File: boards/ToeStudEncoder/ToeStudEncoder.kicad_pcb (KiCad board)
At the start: 2 copper layers, 11 parts, among them J2 ISP, J3 ToeLeft, J4 ToeRight, U1 ATmega48-20P, U2 6N138

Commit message: Renamed toestud encoder schematics
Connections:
- J3 pad 1: Net-(J3-Pad1) -> L1
- J3 pad 10: L3 -> Net-(U1-Pad5)
- J3 pad 2: unconnected-(J3-Pad2) -> Net-(U1-Pad13)
- J3 pad 3: Net-(J3-Pad3) -> unconnected-(J3-Pad3)
- J3 pad 4: unconnected-(J3-Pad4) -> Net-(U1-Pad12)
- J3 pad 5: Net-(J3-Pad5) -> unconnected-(J3-Pad5)
- J3 pad 6: unconnected-(J3-Pad6) -> Net-(U1-Pad11)
- J3 pad 7: Net-(J3-Pad7) -> unconnected-(J3-Pad7)
- J3 pad 8: MOSI -> Net-(U1-Pad6)
- J3 pad 9: Net-(J3-Pad9) -> L2
- J4 pad 1: Net-(J3-Pad1) -> L3
- J4 pad 10: L1 -> Net-(U1-Pad5)
- J4 pad 2: unconnected-(J4-Pad2) -> Net-(U1-Pad13)
- J4 pad 3: Net-(J3-Pad3) -> unconnected-(J4-Pad3)
- J4 pad 4: unconnected-(J4-Pad4) -> Net-(U1-Pad12)
- J4 pad 5: Net-(J3-Pad5) -> unconnected-(J4-Pad5)
- J4 pad 6: unconnected-(J4-Pad6) -> Net-(U1-Pad11)
- J4 pad 7: Net-(J3-Pad7) -> unconnected-(J4-Pad7)
- J4 pad 8: L2 -> Net-(U1-Pad6)
- J4 pad 9: Net-(J3-Pad9) -> MOSI
- U1 pad 11: Net-(J3-Pad5) -> Net-(U1-Pad11)
- U1 pad 12: Net-(J3-Pad7) -> Net-(U1-Pad12)
- U1 pad 13: Net-(J3-Pad9) -> Net-(U1-Pad13)
- U1 pad 5: Net-(J3-Pad1) -> Net-(U1-Pad5)
- U1 pad 6: Net-(J3-Pad3) -> Net-(U1-Pad6)

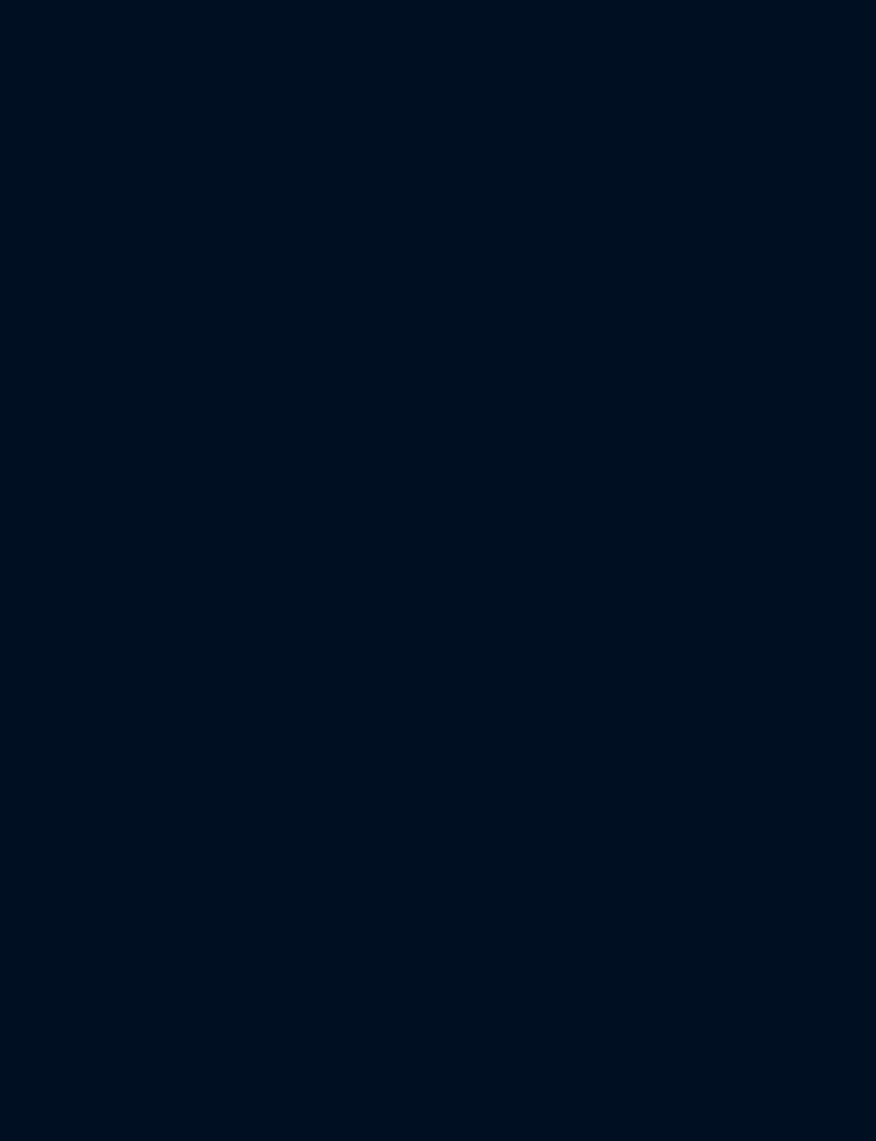
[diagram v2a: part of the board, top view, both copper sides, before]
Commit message: Updated to KiCAD 8, fixed optocouplers for MIDI and added powersupplies
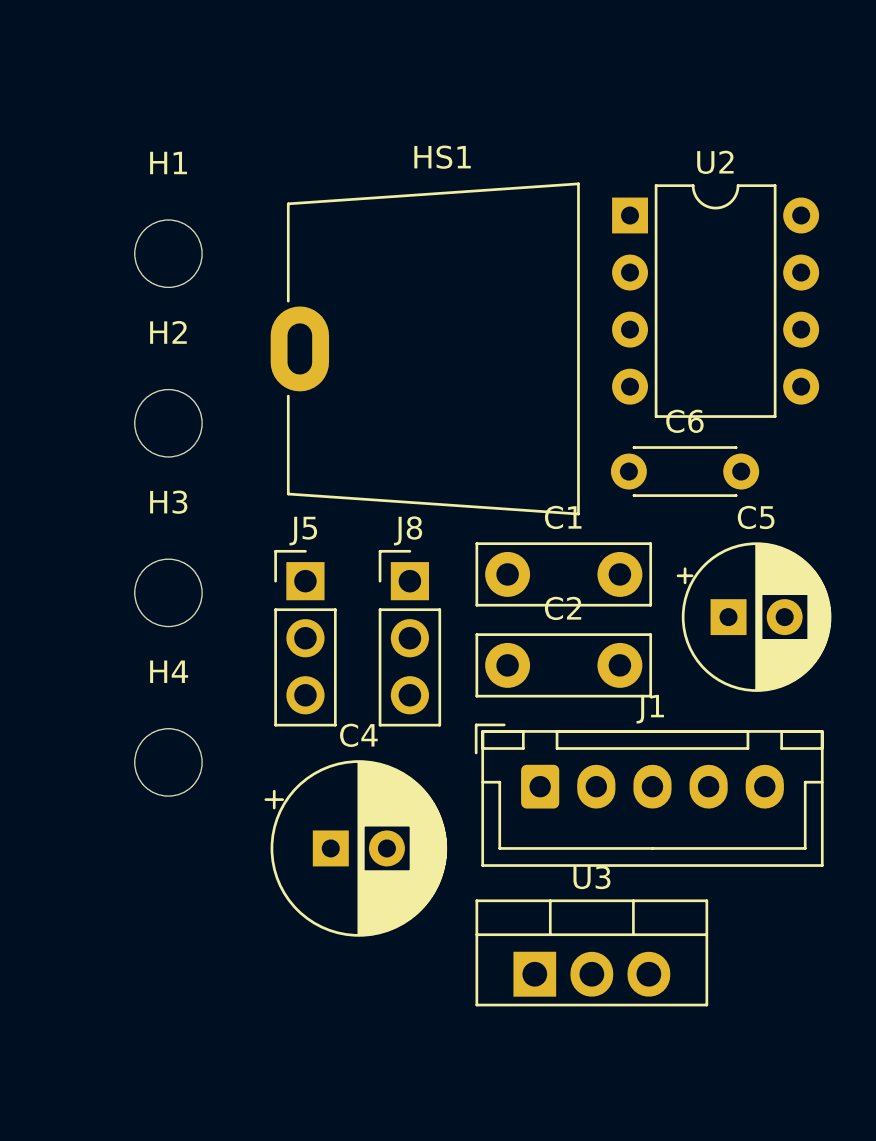
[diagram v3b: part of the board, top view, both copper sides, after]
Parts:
- added C1: 100nF, Capacitor_THT:C_Disc_D7.5mm_W2.5mm_P5.00mm, F.Cu at (233.0, 69.6)
- added C2: 100nF, Capacitor_THT:C_Disc_D7.5mm_W2.5mm_P5.00mm, F.Cu at (233.0, 73.6)
- added C4: 33uF, Capacitor_THT:CP_Radial_D7.5mm_P2.50mm, F.Cu at (225.1, 81.8)
- added C5: 10uF, Capacitor_THT:CP_Radial_D6.3mm_P2.50mm, F.Cu at (242.8, 71.5)
- added C6: 100nF, Capacitor_THT:C_Disc_D4.3mm_W1.9mm_P5.00mm, F.Cu at (238.4, 65.0)
- added H1: MountingHole, MountingHole:MountingHole_3mm, F.Cu at (217.9, 55.3)
- added H2: MountingHole, MountingHole:MountingHole_3mm, F.Cu at (217.9, 62.8)
- added H3: MountingHole, MountingHole:MountingHole_3mm, F.Cu at (217.9, 70.4)
- added H4: MountingHole, MountingHole:MountingHole_3mm, F.Cu at (217.9, 77.9)
- added HS1: Heatsink_Pad, Heatsink:Heatsink_AAVID_576802B03900G, F.Cu at (223.7, 59.5)
- added J1: Swell, Connector_JST:JST_XH_B5B-XH-A_1x05_P2.50mm_Vertical, F.Cu at (234.4, 79.0)
- added J5: MIDI In, Connector_PinHeader_2.54mm:PinHeader_1x03_P2.54mm_Vertical, F.Cu at (224.0, 69.9)
- added J8: MIDI Out, Connector_PinHeader_2.54mm:PinHeader_1x03_P2.54mm_Vertical, F.Cu at (228.6, 69.9)
- added U2: 6N137, Package_DIP:DIP-8_W7.62mm, F.Cu at (238.4, 53.6)
- added U3: L7805, Package_TO_SOT_THT:TO-220-3_Vertical, F.Cu at (234.2, 87.4)
- R1: value 10k -> 1k
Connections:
- D1 pad 1: Net-(D1-Pad1) -> Net-(D1-K)
- D1 pad 2: Net-(D1-Pad2) -> Net-(D1-A)
- R5 pad 2: Net-(D1-Pad1) -> Net-(D1-K)

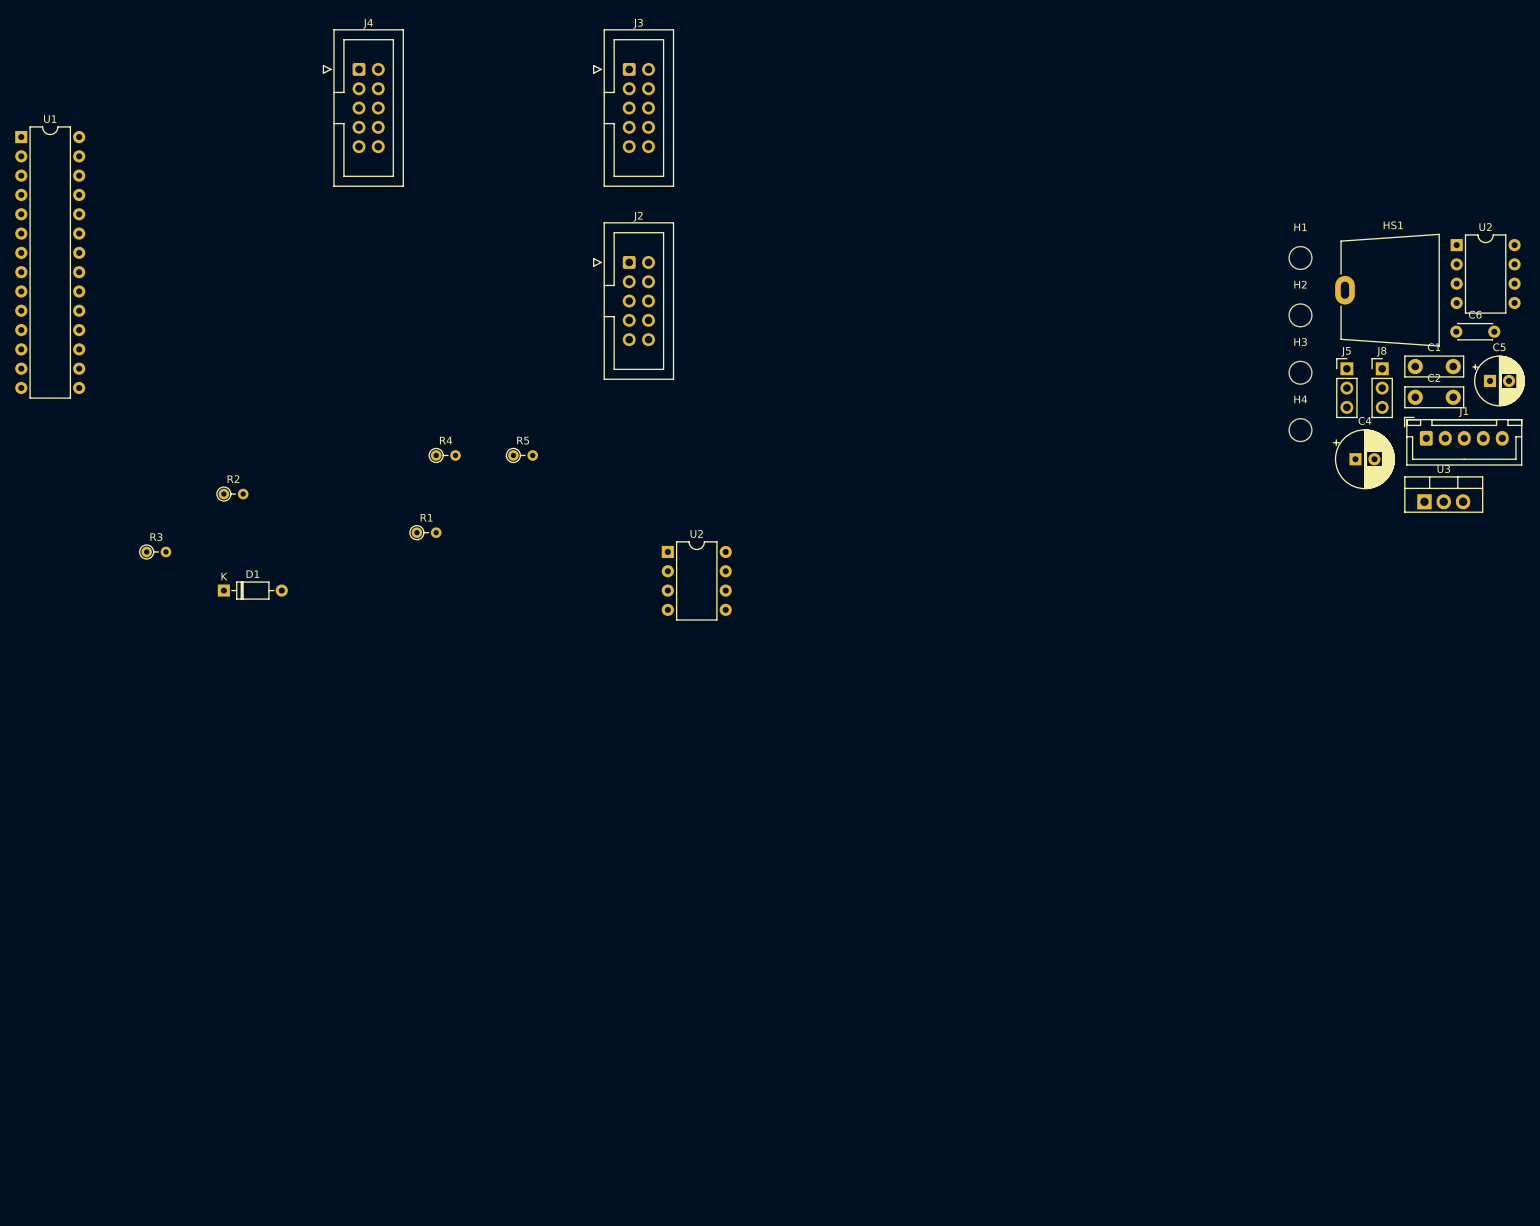
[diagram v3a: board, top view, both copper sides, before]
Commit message: Using custom TO220 cooler, fixed and finished several PCBs
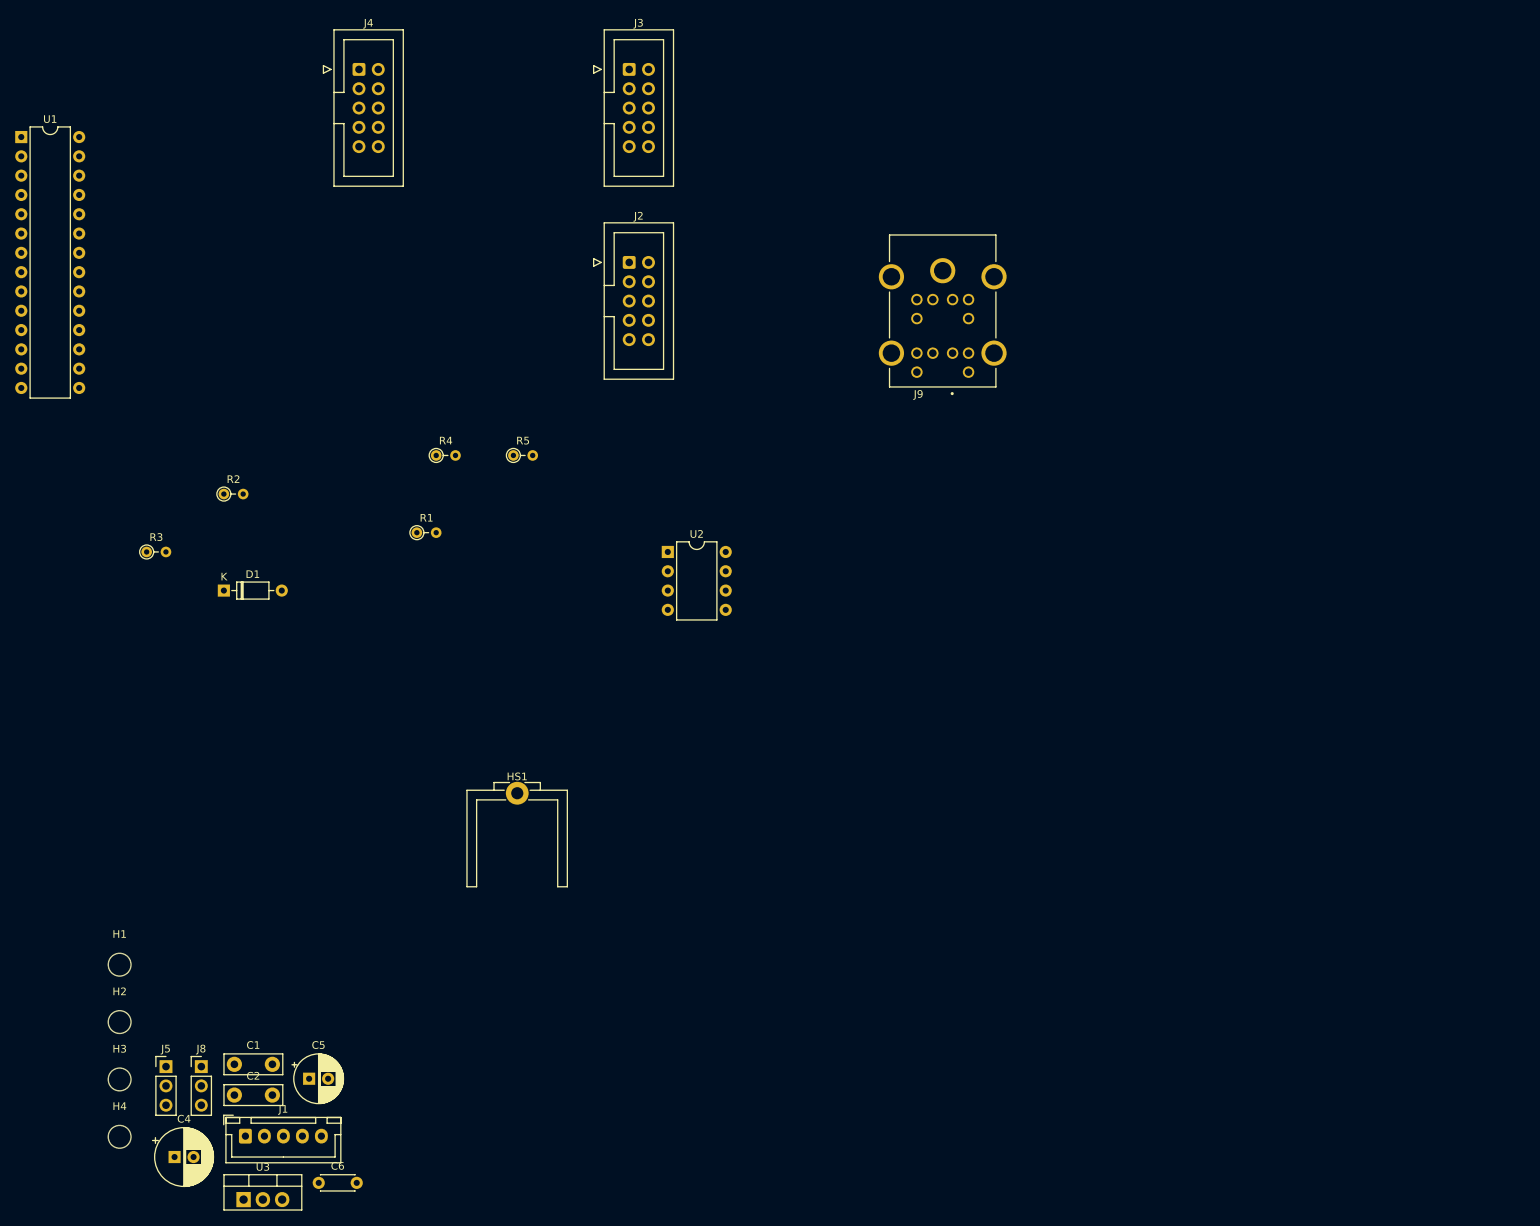
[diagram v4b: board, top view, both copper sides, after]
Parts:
- removed the U2 at (238.4, 53.6)
- added J9: Controller, SnapEDA:SWITCHCRAFT_DMD6FRA111, F.Cu at (170.8, 52.3)
- HS1: footprint Heatsink:Heatsink_AAVID_576802B03900G -> Custom_Heatsinks:Heatsink_Aavid_TO-220_H12.7mm
- U2: value 6N138 -> 6N137
- moved C6 187.0 mm to (88.7, 177.0)
- moved H1 181.1 mm to (62.5, 148.3)
- moved H2 181.1 mm to (62.5, 155.8)
- moved H3 181.1 mm to (62.5, 163.4)
- moved H4 181.1 mm to (62.5, 170.9)
- moved C1 180.5 mm to (77.6, 161.4)
- moved C2 180.5 mm to (77.6, 165.5)
- moved C4 180.5 mm to (69.7, 173.6)
- moved C5 180.5 mm to (87.4, 163.3)
- moved J1 180.5 mm to (79.0, 170.9)
- moved J5 180.5 mm to (68.6, 161.7)
- moved J8 180.5 mm to (73.2, 161.7)
- moved U3 180.5 mm to (78.8, 179.2)
- moved HS1 127.9 mm to (114.8, 126.6)
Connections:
- U2 pad 2: Net-(D1-Pad1) -> Net-(D1-K)
- U2 pad 3: Net-(D1-Pad2) -> Net-(D1-A)

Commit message: Finished PCB for ToeStudEncoder
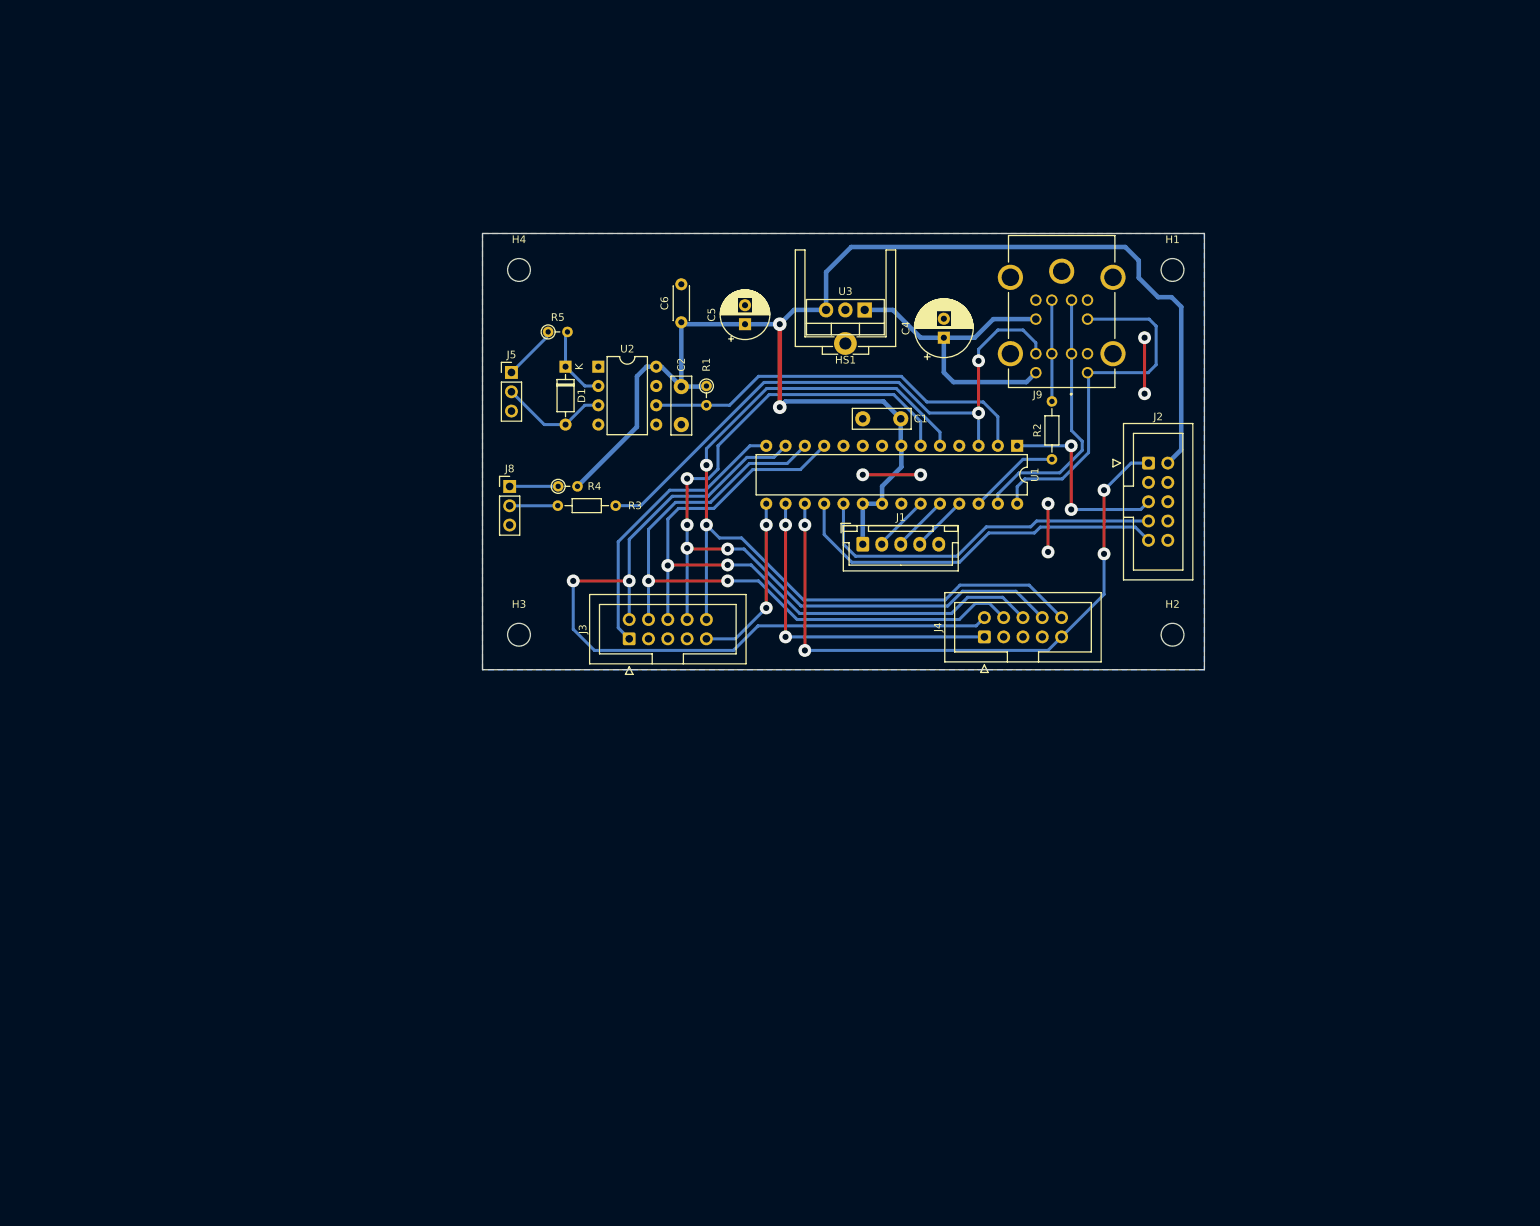
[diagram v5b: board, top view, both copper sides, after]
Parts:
- R2, R3: footprint Resistor_THT:R_Axial_DIN0204_L3.6mm_D1.6mm_P2.54mm_Vertical -> Resistor_THT:R_Axial_DIN0204_L3.6mm_D1.6mm_P7.62mm_Horizontal
- moved H1 166.0 mm to (201.0, 56.9)
- moved C4 147.9 mm to (170.9, 65.8), turned to 90 degrees
- moved H2 147.6 mm to (201.0, 104.9)
- moved U3 142.8 mm to (160.5, 62.1), turned to 180 degrees
- moved U1 137.2 mm to (180.6, 80.0), turned to -90 degrees
- moved H4 125.6 mm to (115.0, 56.9)
- moved C6 122.9 mm to (136.4, 63.8), turned to 90 degrees
- moved C1 122.1 mm to (165.3, 76.5), turned to 180 degrees
- moved C5 114.7 mm to (144.8, 64.0), turned to 90 degrees
- moved J1 112.5 mm to (160.3, 93.0)
- moved J4 111.1 mm to (176.3, 105.2), turned to 90 degrees
- moved C2 110.2 mm to (136.4, 72.2), turned to -90 degrees
- moved R2 109.1 mm to (185.2, 81.8), turned to 90 degrees
- moved J5 102.0 mm to (114.0, 70.4)
- moved J8 86.5 mm to (113.8, 85.4)
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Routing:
- net +5V: track 0.00 -> 184.0 mm, vias 0 -> 2
- net Net-(J3-Pin_10): track 0.00 -> 114.1 mm, vias 0 -> 2
- net Net-(J3-Pin_8): track 0.00 -> 112.5 mm, vias 0 -> 4
- net Net-(J3-Pin_2): track 0.00 -> 107.0 mm, vias 0 -> 2
- net Net-(J3-Pin_6): track 0.00 -> 89.2 mm, vias 0 -> 2
- net Net-(J3-Pin_4): track 0.00 -> 87.5 mm, vias 0 -> 2
- net MOSI: track 0.00 -> 82.8 mm, vias 0 -> 4
- net TXD: track 0.00 -> 79.3 mm, vias 0 -> 2
- net RXD: track 0.00 -> 52.6 mm
- net MISO: track 0.00 -> 50.9 mm
- net SCK: track 0.00 -> 48.0 mm
- net SCL: track 0.00 -> 47.8 mm
- net L3: track 0.00 -> 43.7 mm, vias 0 -> 2
- net +12V: track 0.00 -> 42.8 mm
- net L1: track 0.00 -> 38.1 mm
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- added copper zone on B.Cu, net GND
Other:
- board outline added: 95 x 57.4 mm
